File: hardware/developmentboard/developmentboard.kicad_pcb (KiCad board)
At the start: 2 copper layers, 35 parts, among them J1 SPI Header, J2 Power Header, J3 Hall Effect Header, U1 ADS7960, U10 DRV5053, U11 DRV5053, U12 DRV5053, U13 DRV5053, U14 AP2138N-2.5, U2 DRV5053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

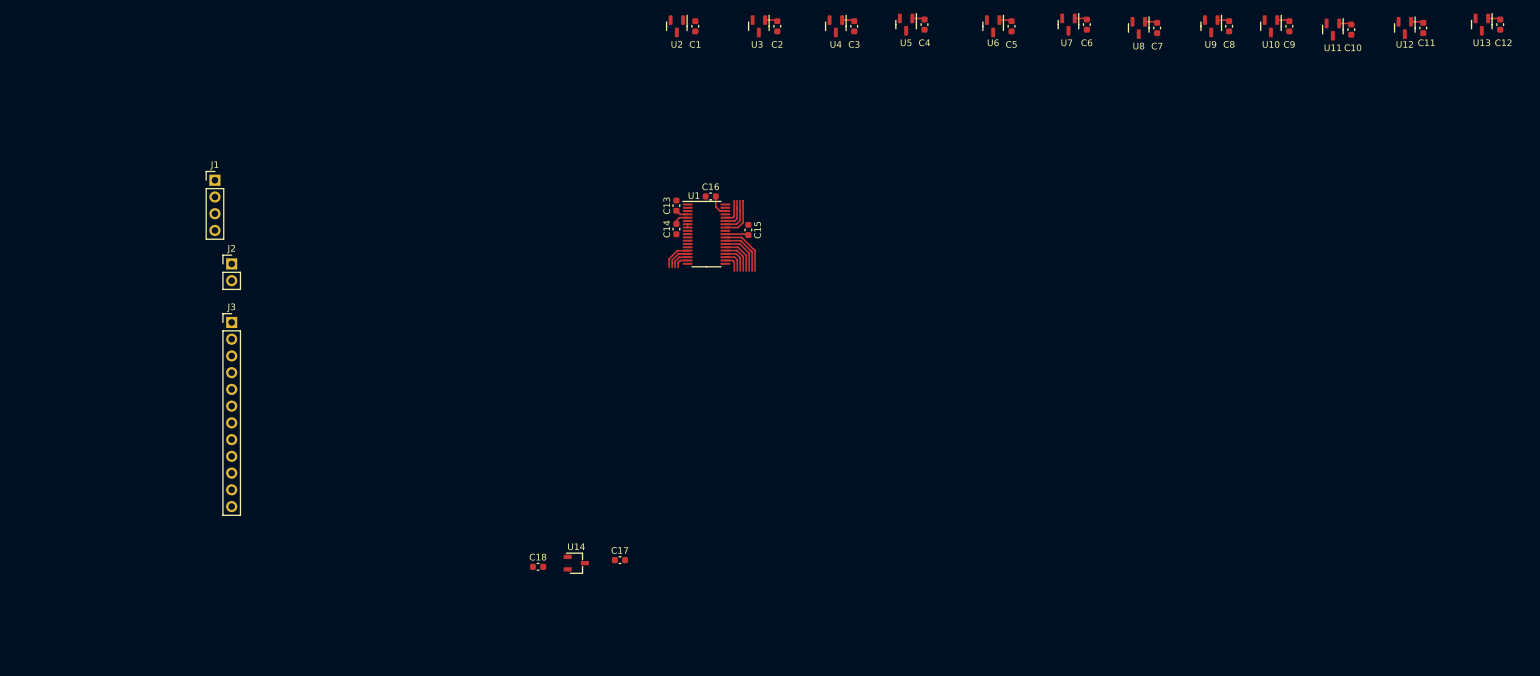
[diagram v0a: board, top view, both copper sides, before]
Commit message: layout for hall effect sensors, imported rules from powerboard
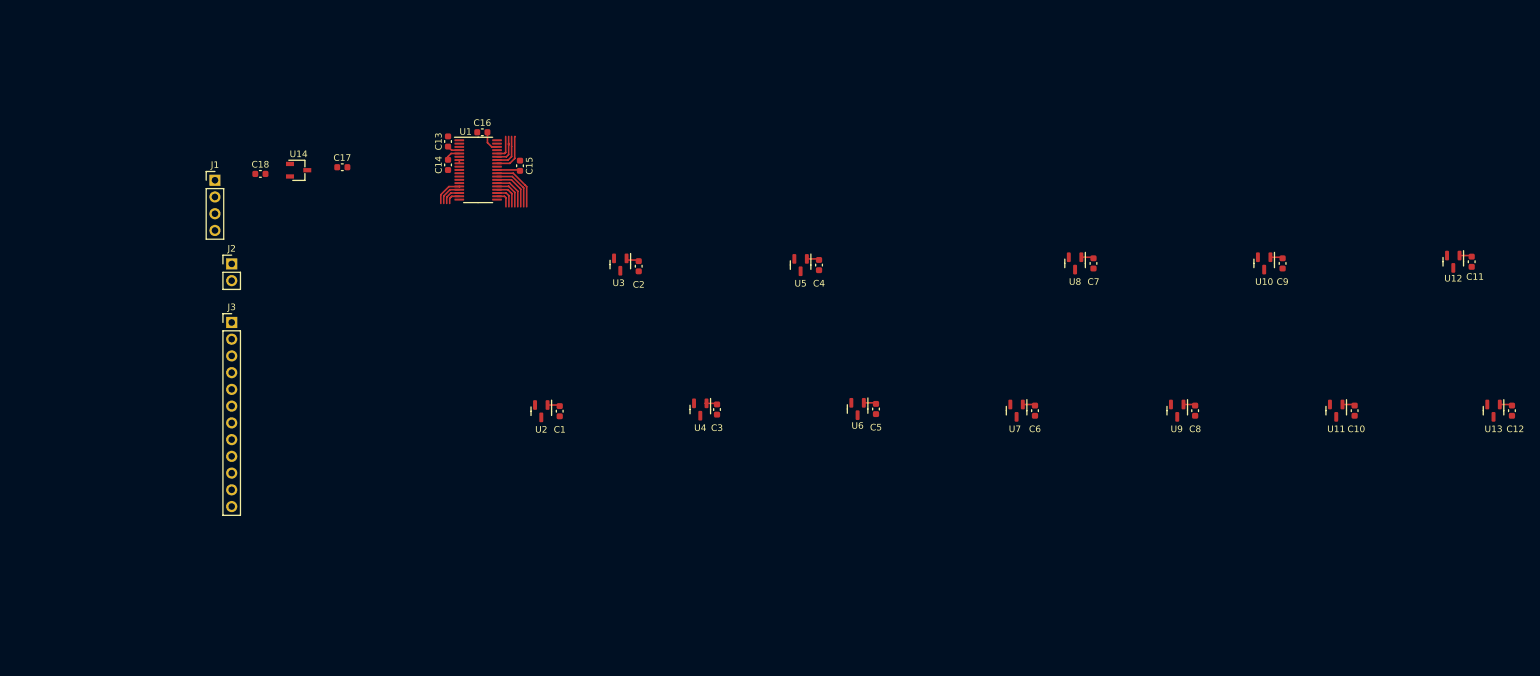
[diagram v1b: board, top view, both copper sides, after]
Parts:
- moved C17 73.0 mm to (103.1, 51.4)
- moved U14 73.0 mm to (96.5, 51.8)
- moved C18 73.0 mm to (90.7, 52.4)
- moved U2 61.9 mm to (133.3, 88.4)
- moved C1 61.9 mm to (136.1, 88.4)
- moved C3 61.8 mm to (160.0, 88.1)
- moved U4 61.7 mm to (157.5, 88.1)
- moved U6 61.6 mm to (181.4, 88.1)
- moved C5 61.6 mm to (184.2, 88.1)
- moved C6 59.1 mm to (208.3, 88.3)
- moved U7 59.1 mm to (205.5, 88.3)
- moved C12 58.6 mm to (280.7, 88.3)
- moved U13 58.6 mm to (277.9, 88.3)
- moved C8 58.6 mm to (232.6, 88.3)
- moved U9 58.6 mm to (229.9, 88.3)
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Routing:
- net +3.3V: track 30.2 -> 32.1 mm

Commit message: routing for keys and ground fill under adc
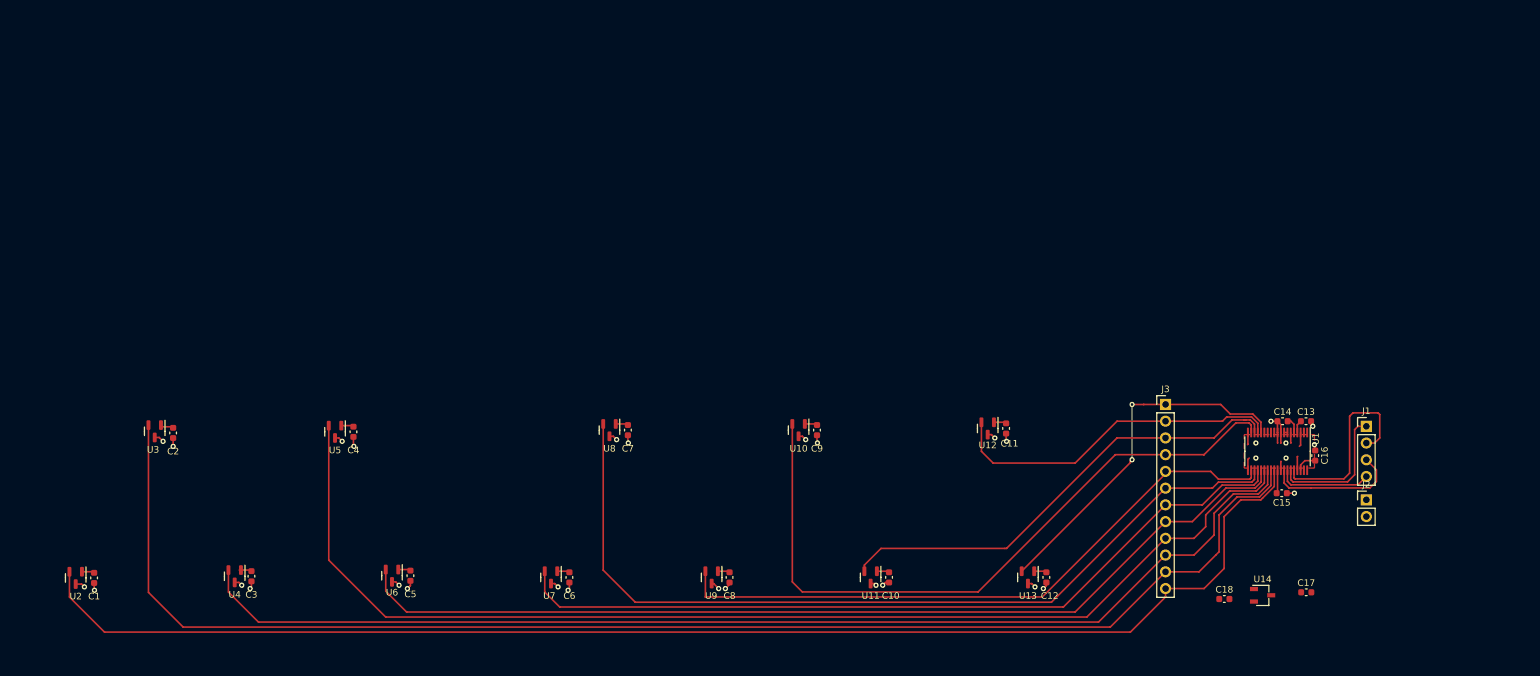
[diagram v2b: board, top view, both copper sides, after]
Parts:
- moved J1 178.7 mm to (258.6, 90.7)
- moved J2 175.9 mm to (258.6, 101.8)
- moved U14 159.9 mm to (242.8, 116.3)
- moved C17 159.9 mm to (249.5, 115.9)
- moved C18 159.9 mm to (237.0, 116.9)
- moved J3 142.3 mm to (228.1, 87.4)
- moved C13 137.0 mm to (249.4, 89.9), turned to 0 degrees
- moved C16 135.6 mm to (250.8, 95.1), turned to -90 degrees
- moved C14 132.5 mm to (245.9, 89.9), turned to 0 degrees
- moved U1 128.6 mm to (245.1, 94.5), turned to -90 degrees
- moved C15 125.8 mm to (245.7, 100.8), turned to 180 degrees
- moved C12 75.1 mm to (210.0, 113.6)
- moved C2 75.1 mm to (77.5, 91.7)
- moved C3 75.1 mm to (89.4, 113.4)
- moved C6 75.1 mm to (137.6, 113.6)
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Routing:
- net CH01: track 7.63 -> 212.4 mm
- net CH00: track 8.40 -> 205.9 mm
- net CH03: track 6.03 -> 177.4 mm
- net CH02: track 6.86 -> 175.7 mm
- net CH04: track 5.28 -> 147.4 mm
- net CH06: track 3.65 -> 132.2 mm
- net CH05: track 4.49 -> 121.9 mm
- net CH08: track 2.35 -> 106.1 mm
- net CH07: track 2.81 -> 96.6 mm
- net CH09: track 3.11 -> 71.0 mm
- net GND: track 0.00 -> 52.1 mm, vias 0 -> 28
- net CH11: track 4.79 -> 54.5 mm, vias 0 -> 2
- net CH10: track 3.88 -> 51.8 mm
- net TX: track 3.81 -> 29.5 mm
- net RX: track 5.04 -> 20.6 mm
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- added copper zone on F.Cu, net GND

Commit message: board outline for developmentboard
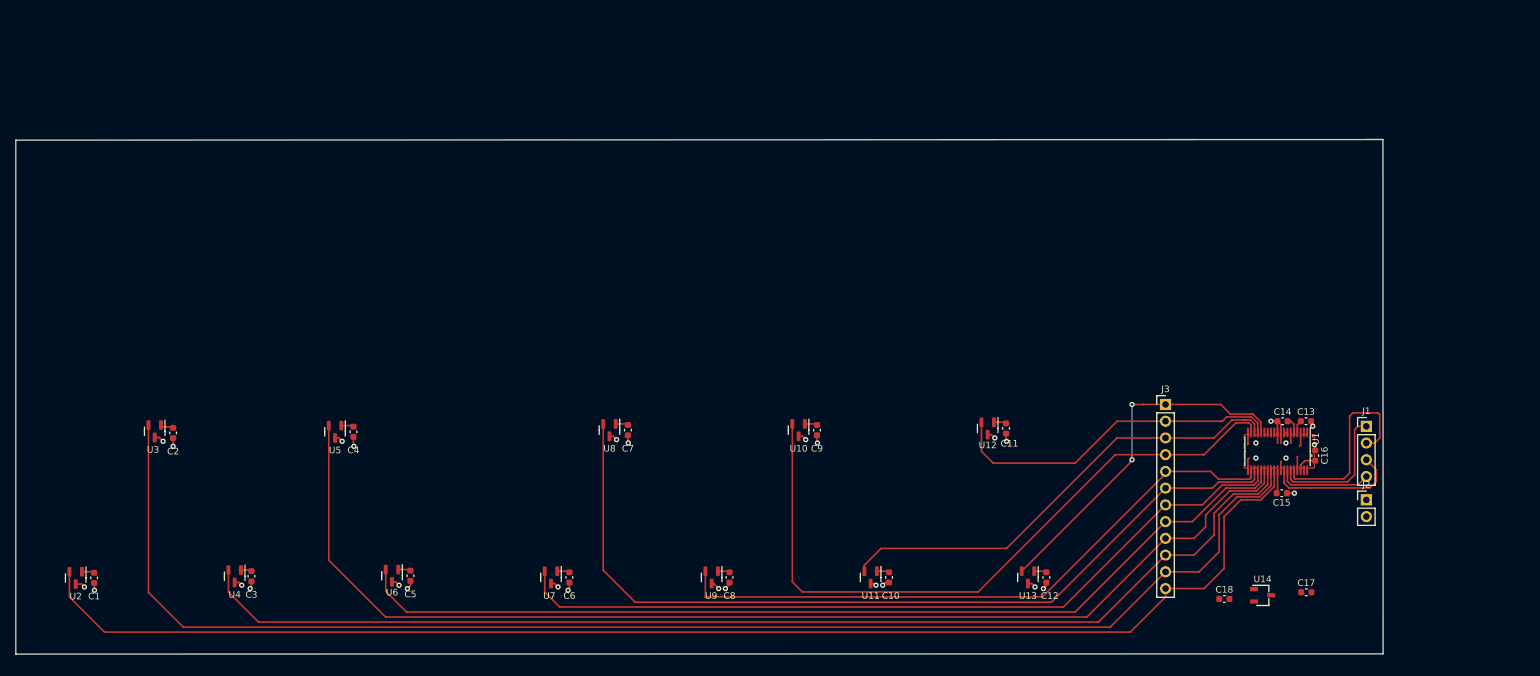
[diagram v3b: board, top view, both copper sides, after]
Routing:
- net GND: vias 28 -> 32
- net (no net): track 0.01 -> 0.00 mm, vias 4 -> 0
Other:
- board outline added: 207.5 x 78.1 mm
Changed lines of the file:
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@@
     )
   )
-  (segment (start 246.38 93.218) (end 246.372582 93.218) (width 0.25) (layer "F.Cu") (net 0))
-  (segment (start 246.372582 93.218) (end 246.37206 93.218522) (width 0.25) (layer "F.Cu") (net 0))
-  (via (at 246.37206 93.218522) (size 0.8) (drill 0.4) (layers "F.Cu" "B.Cu") (net 0))
-  (via (at 246.38 95.504) (size 0.8) (drill 0.4) (layers "F.Cu" "B.Cu") (net 0))
-  (via (at 241.808 95.504) (size 0.8) (drill 0.4) (layers "F.Cu" "B.Cu") (net 0))
-  (via (at 241.808 93.218) (size 0.8) (drill 0.4) (layers "F.Cu" "B.Cu") (net 0))
+  (gr_line (start 261.094 47.156) (end 261.112 125.222) (layer "Edge.Cuts") (width 0.1))
+  (gr_line (start 261.112 125.222) (end 53.594 125.256) (layer "Edge.Cuts") (width 0.1))
+  (gr_line (start 53.594 125.256) (end 53.594 47.256) (layer "Edge.Cuts") (width 0.1))
+  (gr_line (start 53.594 47.256) (end 261.094 47.156) (layer "Edge.Cuts") (width 0.1))
   (segment (start 183.33475 114.554) (end 183.896 114.554) (width 0.25) (layer "F.Cu") (net 1))
   (segment (start 159.512 114.554) (end 160.274 115.316) (width 0.25) (layer "F.Cu") (net 1))
@@
   (segment (start 175.26 93.096) (end 175.194 93.03) (width 0.25) (layer "F.Cu") (net 1))
   (segment (start 240.595 91.6255) (end 240.595 93.415) (width 0.25) (layer "F.Cu") (net 1))
+  (segment (start 246.38 93.218) (end 246.372582 93.218) (width 0.25) (layer "F.Cu") (net 1))
   (segment (start 102.042 92.456) (end 102.616 92.456) (width 0.25) (layer "F.Cu") (net 1))
   (segment (start 110.69075 114.3) (end 111.252 114.3) (width 0.25) (layer "F.Cu") (net 1))
@@
   (segment (start 245.595 97.3505) (end 245.595 96.035) (width 0.25) (layer "F.Cu") (net 1))
   (segment (start 113.48475 114.1375) (end 113.48475 114.86125) (width 0.25) (layer "F.Cu") (net 1))
+  (segment (start 246.372582 93.218) (end 246.37206 93.218522) (width 0.25) (layer "F.Cu") (net 1))
   (segment (start 135.382 114.554) (end 135.89 115.062) (width 0.25) (layer "F.Cu") (net 1))
   (segment (start 250.188 89.916) (end 250.188 90.422) (width 0.25) (layer "F.Cu") (net 1))
@@
   (via (at 77.47 93.726) (size 0.8) (drill 0.4) (layers "F.Cu" "B.Cu") (net 1))
   (via (at 175.26 93.218) (size 0.8) (drill 0.4) (layers "F.Cu" "B.Cu") (net 1))
+  (via (at 246.37206 93.218522) (size 0.8) (drill 0.4) (layers "F.Cu" "B.Cu") (net 1))
   (via (at 65.532 115.57) (size 0.8) (drill 0.4) (layers "F.Cu" "B.Cu") (net 1))
   (via (at 103.124 92.964) (size 0.8) (drill 0.4) (layers "F.Cu" "B.Cu") (net 1))
@@
   (via (at 250.698 93.472) (size 0.8) (drill 0.4) (layers "F.Cu" "B.Cu") (net 1))
   (via (at 135.89 115.062) (size 0.8) (drill 0.4) (layers "F.Cu" "B.Cu") (net 1))
+  (via (at 246.38 95.504) (size 0.8) (drill 0.4) (layers "F.Cu" "B.Cu") (net 1))
   (via (at 113.03 115.316) (size 0.8) (drill 0.4) (layers "F.Cu" "B.Cu") (net 1))
   (via (at 250.444 90.678) (size 0.8) (drill 0.4) (layers "F.Cu" "B.Cu") (net 1))
@@
   (via (at 144.78 92.71) (size 0.8) (drill 0.4) (layers "F.Cu" "B.Cu") (net 1))
   (via (at 208.28 115.062) (size 0.8) (drill 0.4) (layers "F.Cu" "B.Cu") (net 1))
+  (via (at 241.808 95.504) (size 0.8) (drill 0.4) (layers "F.Cu" "B.Cu") (net 1))
   (via (at 64.008 115.062) (size 0.8) (drill 0.4) (layers "F.Cu" "B.Cu") (net 1))
   (via (at 244.094 89.916) (size 0.8) (drill 0.4) (layers "F.Cu" "B.Cu") (net 1))
+  (via (at 241.808 93.218) (size 0.8) (drill 0.4) (layers "F.Cu" "B.Cu") (net 1))
   (via (at 146.558 93.218) (size 0.8) (drill 0.4) (layers "F.Cu" "B.Cu") (net 1))
   (via (at 161.29 115.316) (size 0.8) (drill 0.4) (layers "F.Cu" "B.Cu") (net 1))

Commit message: fized DRC errors
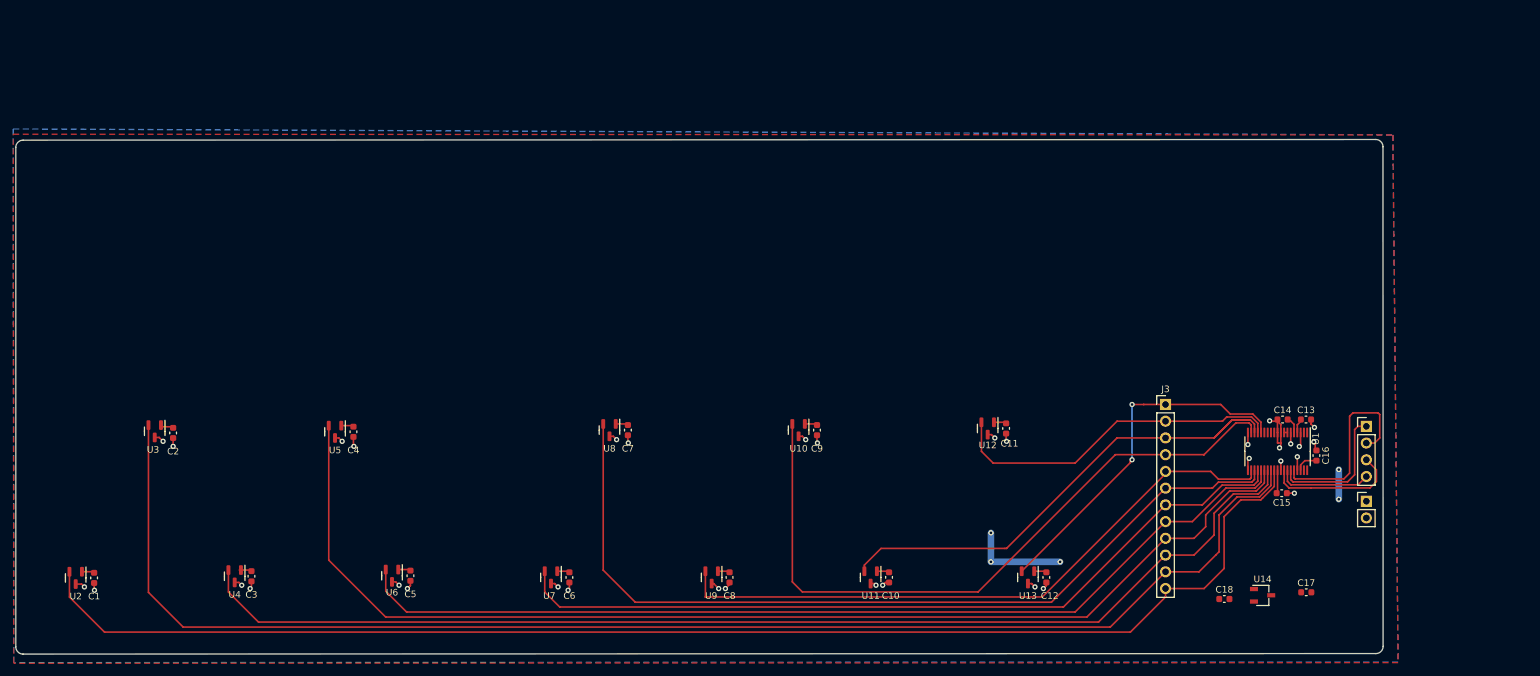
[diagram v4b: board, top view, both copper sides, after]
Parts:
- moved C13 0.26 mm to (249.4, 89.7)
- moved C14 0.26 mm to (245.9, 89.7)
- moved J2 0.21 mm to (258.6, 102.1)
- moved C16 0.18 mm to (251.0, 95.1)
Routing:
- net +3.3V: track 32.1 -> 51.5 mm, vias 0 -> 5
- net CH09: track 71.0 -> 77.3 mm
- net GND: track 52.1 -> 54.4 mm, vias 32 -> 35
- added copper zone on F.Cu, net +3.3V
- added copper zone on B.Cu, net GND
- removed copper zone on F.Cu, net GND
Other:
- outline, holes or cut-outs redrawn

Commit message: added more to silkscreen on developmentboard
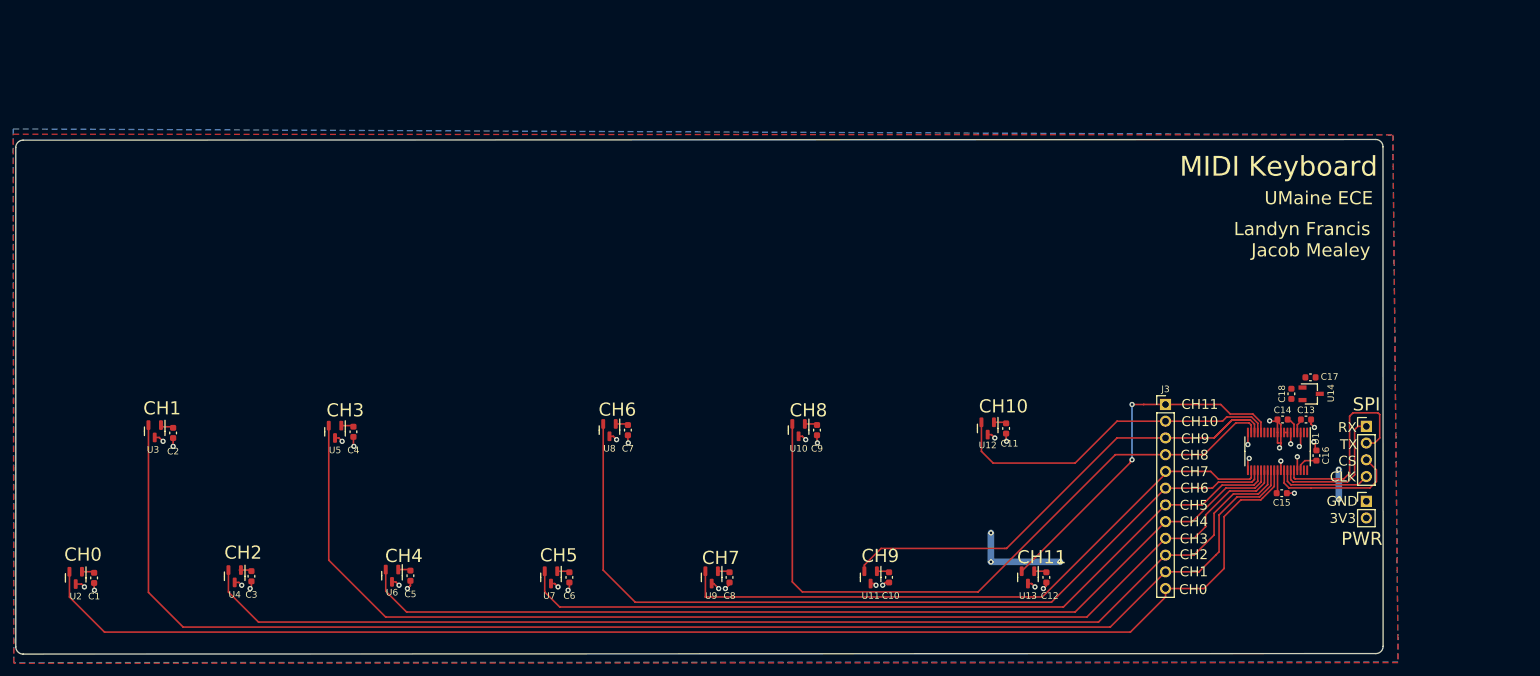
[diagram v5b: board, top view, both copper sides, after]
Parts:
- J3: value Hall Effect Header -> Key Channels
- moved C18 32.8 mm to (247.2, 85.8), turned to 90 degrees
- moved C17 32.6 mm to (250.1, 83.3), turned to 180 degrees
- moved U14 31.5 mm to (250.2, 85.8)
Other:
- board text added: "3V3"
- board text added: "CH0"
- board text added: "CH1"
- board text added: "CH10"
- board text added: "CH11"
- board text added: "CH2"
- board text added: "CH3"
- board text added: "CH4"
- board text added: "CH5"
- board text added: "CH6"
- board text added: "CH7"
- board text added: "CH8"
- board text added: "CH9"
- board text added: "CLK"
- board text added: "CS"
- board text added: "Designed in Orono ME"
- board text added: "GND"
- board text added: "Landyn Francis Jacob Mealey"
- board text added: "MIDI Keyboard"
- board text added: "PWR"
- board text added: "REV 1"
- board text added: "RX"
- board text added: "SPI"
- board text added: "TX"
- board text added: "UMaine ECE"
